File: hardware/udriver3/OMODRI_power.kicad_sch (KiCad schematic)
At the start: 7 parts, among them U7 TMS320F28388D

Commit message: PCB updates. - Replace CAN/RS485 120ohm resistor - Replace resistor on TCAN RXD pin - Update of some references - Add some 3D missing models
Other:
- sheet OMODRI_Alim_12V ports: added none; removed PG_12V0
- sheet OMODRI_Alim_5V ports: added none; removed PG_12V0
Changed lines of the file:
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@@
-    (stroke (width 0) (type default) (color 0 0 0 0))
-  )
-  (wire (pts (xy 49.53 81.28) (xy 58.42 81.28))
     (stroke (width 0) (type default) (color 0 0 0 0))
   )
@@
     )
     (property "Sheet file" "OMODRI_Alim_5V.kicad_sch" (id 1) (at 58.42 88.2146 0)
-      (effects (font (size 1.27 1.27)) (justify left top))
+      (effects (font (size 1.27 1.27)) (justify left top) hide)
     )
     (pin "PG_5V0" output (at 83.82 81.28 0)
       (effects (font (size 1.27 1.27)) (justify right))
-    )
-    (pin "PG_12V0" input (at 58.42 81.28 180)
-      (effects (font (size 1.27 1.27)) (justify left))
     )
   )
@@
     )
     (property "Sheet file" "OMODRI_Alim_3V3.kicad_sch" (id 1) (at 93.98 77.47 0)
-      (effects (font (size 1.27 1.27)) (justify left top))
+      (effects (font (size 1.27 1.27)) (justify left top) hide)
     )
     (pin "PG_5V0" input (at 93.98 76.2 180)
@@
     )
     (property "Sheet file" "OMODRI_Alim_1V2.kicad_sch" (id 1) (at 93.98 87.5796 0)
-      (effects (font (size 1.27 1.27)) (justify left top))
+      (effects (font (size 1.27 1.27)) (justify left top) hide)
     )
     (pin "PG_5V0" input (at 93.98 85.09 180)
@@
     )
     (property "Sheet file" "OMODRI_Alim_REF.kicad_sch" (id 1) (at 93.98 96.52 0)
-      (effects (font (size 1.27 1.27)) (justify left top))
+      (effects (font (size 1.27 1.27)) (justify left top) hide)
     )
   )
@@
     )
     (property "Sheet file" "TMS320_Bypass_Cap.kicad_sch" (id 1) (at 93.98 107.95 0)
-      (effects (font (size 1.27 1.27)) (justify left top))
+      (effects (font (size 1.27 1.27)) (justify left top) hide)
     )
   )
@@
     )
     (property "Sheet file" "OMODRI_Alim_12V.kicad_sch" (id 1) (at 24.13 88.2146 0)
-      (effects (font (size 1.27 1.27)) (justify left top))
-    )
-    (pin "PG_12V0" output (at 49.53 81.28 0)
-      (effects (font (size 1.27 1.27)) (justify right))
-    )
-  )
+      (effects (font (size 1.27 1.27)) (justify left top) hide)
+    )
+  )

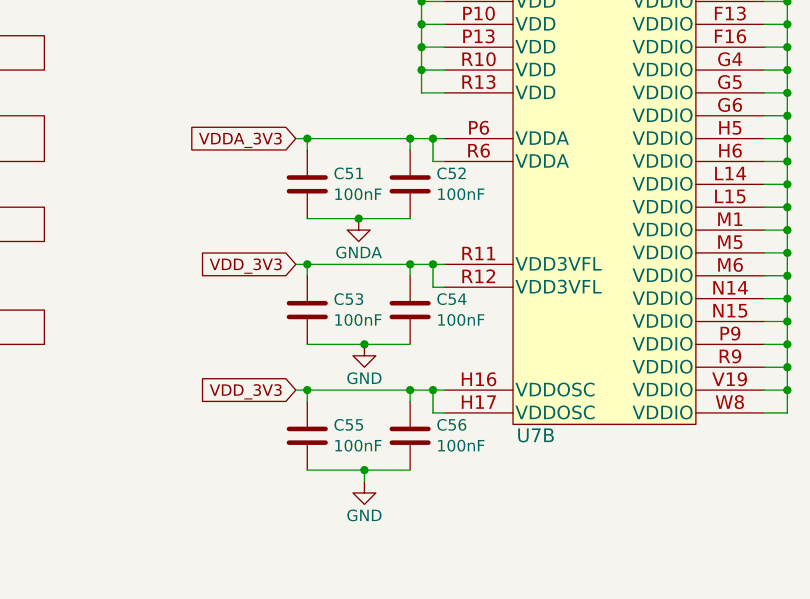
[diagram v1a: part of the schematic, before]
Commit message: PCB updates - FSI protection added against FPC cable reverse connection - BOSCH BMI088 IMU added.
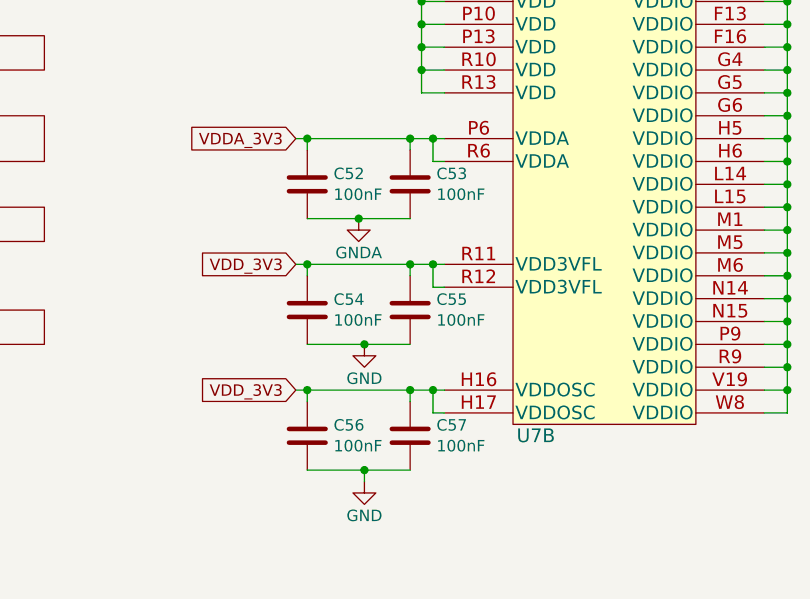
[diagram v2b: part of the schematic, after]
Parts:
- renumbered C51 to C52, C52 to C53, C53 to C54, C54 to C55, C55 to C56, C56 to C57
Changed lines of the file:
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@@
   (title_block
     (title "Open MOtor DRiver Initiative (OMODRI)")
-    (date "2022-10-05")
+    (date "2022-11-24")
     (rev "2.0")
     (company "LAAS/CNRS")
@@
   (symbol (lib_id "power:GND") (at 214.63 143.51 0) (unit 1)
     (in_bom yes) (on_board yes)
-    (property "Reference" "#PWR0122" (id 0) (at 214.63 149.86 0)
+    (property "Reference" "#PWR0123" (id 0) (at 214.63 149.86 0)
       (effects (font (size 1.27 1.27)) hide)
     )
@@
   (symbol (lib_id "power:GND") (at 252.73 143.51 0) (unit 1)
     (in_bom yes) (on_board yes)
-    (property "Reference" "#PWR0123" (id 0) (at 252.73 149.86 0)
+    (property "Reference" "#PWR0124" (id 0) (at 252.73 149.86 0)
       (effects (font (size 1.27 1.27)) hide)
     )
@@
   (symbol (lib_id "power:GND") (at 153.67 107.95 0) (unit 1)
     (in_bom yes) (on_board yes)
-    (property "Reference" "#PWR0120" (id 0) (at 153.67 114.3 0)
+    (property "Reference" "#PWR0121" (id 0) (at 153.67 114.3 0)
       (effects (font (size 1.27 1.27)) hide)
     )
@@
   (symbol (lib_id "power:GND") (at 153.67 123.19 0) (unit 1)
     (in_bom yes) (on_board yes)
-    (property "Reference" "#PWR0121" (id 0) (at 153.67 129.54 0)
+    (property "Reference" "#PWR0122" (id 0) (at 153.67 129.54 0)
       (effects (font (size 1.27 1.27)) hide)
     )
@@
   (symbol (lib_id "power:GNDA") (at 153.035 93.98 0) (unit 1)
     (in_bom yes) (on_board yes)
-    (property "Reference" "#PWR0119" (id 0) (at 153.035 100.33 0)
+    (property "Reference" "#PWR0120" (id 0) (at 153.035 100.33 0)
       (effects (font (size 1.27 1.27)) hide)
     )
@@
   (symbol (lib_id "Device:C") (at 147.32 118.11 0) (unit 1)
     (in_bom yes) (on_board yes)
-    (property "Reference" "C55" (id 0) (at 150.241 116.9416 0)
+    (property "Reference" "C56" (id 0) (at 150.241 116.9416 0)
       (effects (font (size 1.27 1.27)) (justify left))
     )
@@
   (symbol (lib_id "Device:C") (at 147.32 104.14 0) (unit 1)
     (in_bom yes) (on_board yes)
-    (property "Reference" "C53" (id 0) (at 150.241 102.9716 0)
+    (property "Reference" "C54" (id 0) (at 150.241 102.9716 0)
       (effects (font (size 1.27 1.27)) (justify left))
     )
@@
   (symbol (lib_id "Device:C") (at 147.32 90.17 0) (unit 1)
     (in_bom yes) (on_board yes)
-    (property "Reference" "C51" (id 0) (at 150.241 89.0016 0)
+    (property "Reference" "C52" (id 0) (at 150.241 89.0016 0)
       (effects (font (size 1.27 1.27)) (justify left))
     )
@@
   (symbol (lib_id "Device:C") (at 158.75 104.14 0) (unit 1)
     (in_bom yes) (on_board yes)
-    (property "Reference" "C54" (id 0) (at 161.671 102.9716 0)
+    (property "Reference" "C55" (id 0) (at 161.671 102.9716 0)
       (effects (font (size 1.27 1.27)) (justify left))
     )
@@
   (symbol (lib_id "Device:C") (at 158.75 118.11 0) (unit 1)
     (in_bom yes) (on_board yes)
-    (property "Reference" "C56" (id 0) (at 161.671 116.9416 0)
+    (property "Reference" "C57" (id 0) (at 161.671 116.9416 0)
       (effects (font (size 1.27 1.27)) (justify left))
     )
@@
   (symbol (lib_id "Device:C") (at 158.75 90.17 0) (unit 1)
     (in_bom yes) (on_board yes)
-    (property "Reference" "C52" (id 0) (at 161.671 89.0016 0)
+    (property "Reference" "C53" (id 0) (at 161.671 89.0016 0)
       (effects (font (size 1.27 1.27)) (justify left))
     )

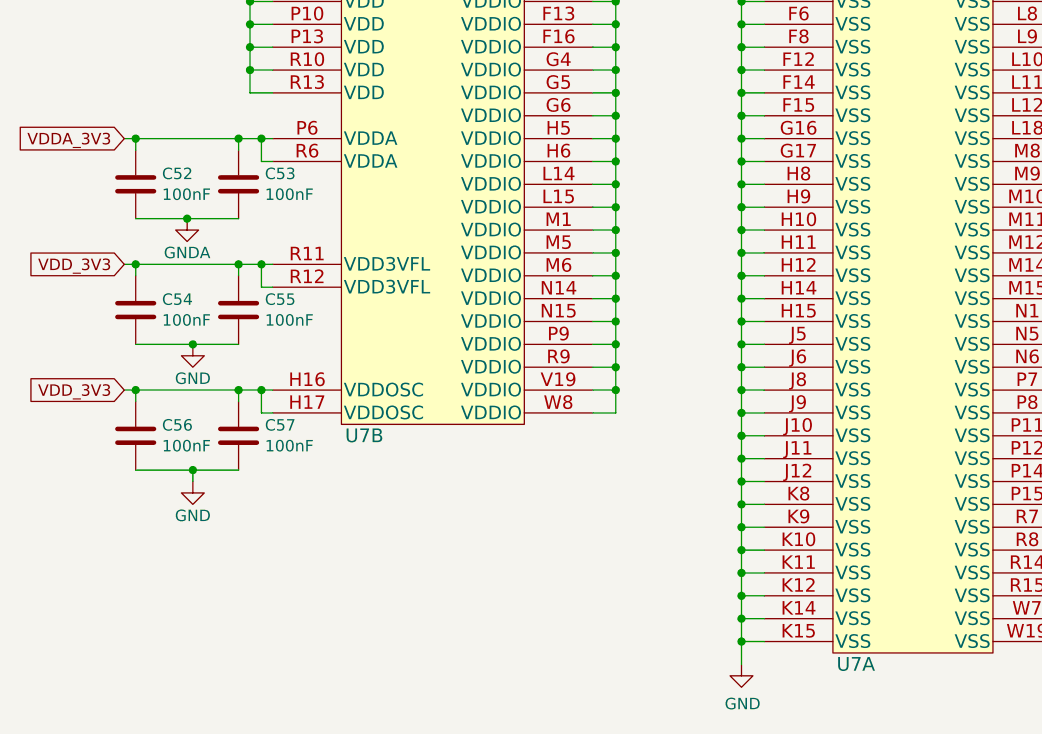
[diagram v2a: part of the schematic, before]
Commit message: PCB udpates. - add serial resistors on boot jumpers - modify config jumpers to be opened by default
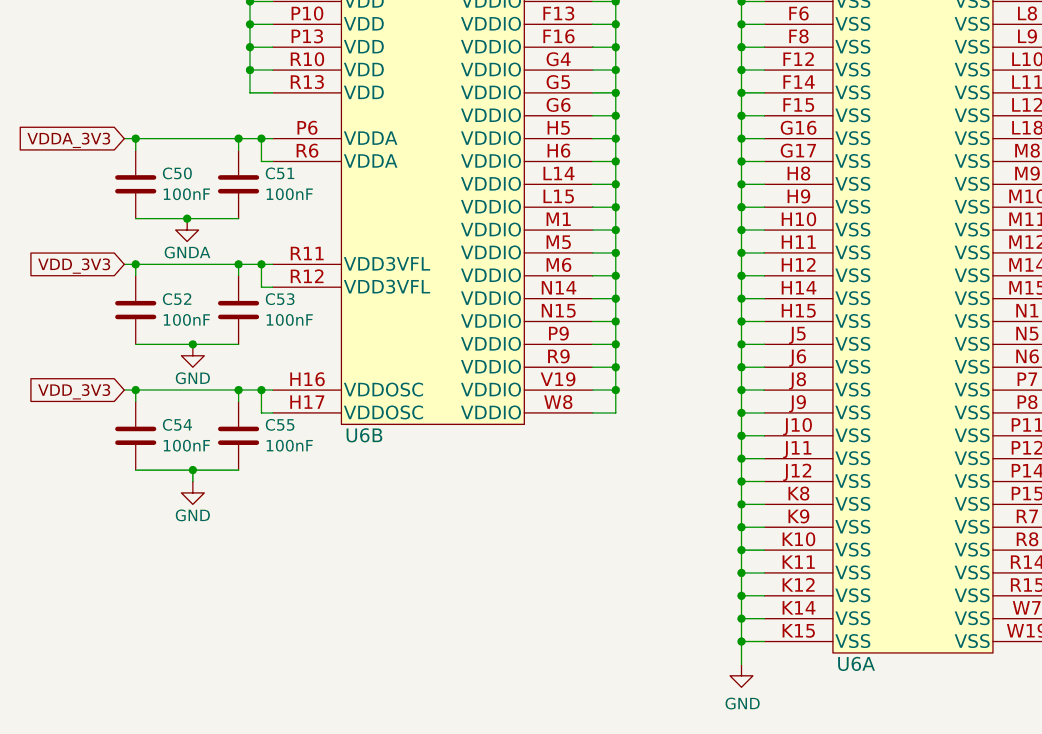
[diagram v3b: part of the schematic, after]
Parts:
- renumbered C52 to C50, C53 to C51, C54 to C52, C55 to C53, C56 to C54, C57 to C55, U7 to U6
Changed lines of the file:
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@@
   (symbol (lib_id "power:GND") (at 214.63 143.51 0) (unit 1)
     (in_bom yes) (on_board yes)
-    (property "Reference" "#PWR0123" (id 0) (at 214.63 149.86 0)
+    (property "Reference" "#PWR0109" (id 0) (at 214.63 149.86 0)
       (effects (font (size 1.27 1.27)) hide)
     )
@@
   (symbol (lib_id "power:GND") (at 252.73 143.51 0) (unit 1)
     (in_bom yes) (on_board yes)
-    (property "Reference" "#PWR0124" (id 0) (at 252.73 149.86 0)
+    (property "Reference" "#PWR0110" (id 0) (at 252.73 149.86 0)
       (effects (font (size 1.27 1.27)) hide)
     )
@@
     (pin "1")
   )
-  (symbol (lib_id "omodri_lib:TMS320F28388D") (at 180.34 95.25 0) (unit 2)
-    (in_bom yes) (on_board yes)
-    (property "Reference" "U7" (id 0) (at 172.72 118.11 0)
+  (symbol (lib_name "TMS320F28388D_1") (lib_id "omodri_lib:TMS320F28388D") (at 180.34 95.25 0) (unit 2)
+    (in_bom yes) (on_board yes)
+    (property "Reference" "U6" (id 0) (at 172.72 118.11 0)
       (effects (font (size 1.524 1.524)))
     )
@@
   (symbol (lib_id "omodri_lib:TMS320F28388D") (at 233.68 95.25 0) (unit 1)
     (in_bom yes) (on_board yes)
-    (property "Reference" "U7" (id 0) (at 227.33 143.51 0)
+    (property "Reference" "U6" (id 0) (at 227.33 143.51 0)
       (effects (font (size 1.524 1.524)))
     )
@@
   (symbol (lib_id "power:GND") (at 153.67 107.95 0) (unit 1)
     (in_bom yes) (on_board yes)
-    (property "Reference" "#PWR0121" (id 0) (at 153.67 114.3 0)
+    (property "Reference" "#PWR0107" (id 0) (at 153.67 114.3 0)
       (effects (font (size 1.27 1.27)) hide)
     )
@@
   (symbol (lib_id "power:GND") (at 153.67 123.19 0) (unit 1)
     (in_bom yes) (on_board yes)
-    (property "Reference" "#PWR0122" (id 0) (at 153.67 129.54 0)
+    (property "Reference" "#PWR0108" (id 0) (at 153.67 129.54 0)
       (effects (font (size 1.27 1.27)) hide)
     )
@@
   (symbol (lib_id "power:GNDA") (at 153.035 93.98 0) (unit 1)
     (in_bom yes) (on_board yes)
-    (property "Reference" "#PWR0120" (id 0) (at 153.035 100.33 0)
+    (property "Reference" "#PWR0106" (id 0) (at 153.035 100.33 0)
       (effects (font (size 1.27 1.27)) hide)
     )
@@
   (symbol (lib_id "Device:C") (at 147.32 118.11 0) (unit 1)
     (in_bom yes) (on_board yes)
-    (property "Reference" "C56" (id 0) (at 150.241 116.9416 0)
+    (property "Reference" "C54" (id 0) (at 150.241 116.9416 0)
       (effects (font (size 1.27 1.27)) (justify left))
     )
@@
   (symbol (lib_id "Device:C") (at 147.32 104.14 0) (unit 1)
     (in_bom yes) (on_board yes)
-    (property "Reference" "C54" (id 0) (at 150.241 102.9716 0)
+    (property "Reference" "C52" (id 0) (at 150.241 102.9716 0)
       (effects (font (size 1.27 1.27)) (justify left))
     )
@@
   (symbol (lib_id "Device:C") (at 147.32 90.17 0) (unit 1)
     (in_bom yes) (on_board yes)
-    (property "Reference" "C52" (id 0) (at 150.241 89.0016 0)
+    (property "Reference" "C50" (id 0) (at 150.241 89.0016 0)
       (effects (font (size 1.27 1.27)) (justify left))
     )
@@
   (symbol (lib_id "Device:C") (at 158.75 104.14 0) (unit 1)
     (in_bom yes) (on_board yes)
-    (property "Reference" "C55" (id 0) (at 161.671 102.9716 0)
+    (property "Reference" "C53" (id 0) (at 161.671 102.9716 0)
       (effects (font (size 1.27 1.27)) (justify left))
     )
@@
   (symbol (lib_id "Device:C") (at 158.75 118.11 0) (unit 1)
     (in_bom yes) (on_board yes)
-    (property "Reference" "C57" (id 0) (at 161.671 116.9416 0)
+    (property "Reference" "C55" (id 0) (at 161.671 116.9416 0)
       (effects (font (size 1.27 1.27)) (justify left))
     )
@@
   (symbol (lib_id "Device:C") (at 158.75 90.17 0) (unit 1)
     (in_bom yes) (on_board yes)
-    (property "Reference" "C53" (id 0) (at 161.671 89.0016 0)
-      (effects (font (size 1.27 1.27)) (justify left))
-    )
+    (property "Reference" "C51" (id 0) (at 161.671 89.0016 0)
+      (effects (font (size 1.27 1.27)) (justify left))
+    )

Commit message: Gerber updates.
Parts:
- U6: DigiKey 296-F28388DZWTS-ND -> 296-F28388DZWTS-ND
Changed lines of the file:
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@@
       (effects (font (size 1.524 1.524)) hide)
     )
-    (property "DigiKey" " 	296-F28388DZWTS-ND" (id 4) (at 180.34 95.25 0)
+    (property "DigiKey" "296-F28388DZWTS-ND" (id 4) (at 180.34 95.25 0)
       (effects (font (size 1.27 1.27)) hide)
     )
@@
       (effects (font (size 1.524 1.524)) hide)
     )
-    (property "DigiKey" " 	296-F28388DZWTS-ND" (id 4) (at 233.68 95.25 0)
+    (property "DigiKey" "296-F28388DZWTS-ND" (id 4) (at 233.68 95.25 0)
       (effects (font (size 1.27 1.27)) hide)
     )

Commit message: Add JLCPCB components ref where it was matching.
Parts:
- C50, C51, C52, C53, C54, C55: LCSC (none) -> C2649540
- U6: LCSC (none) -> C2879671
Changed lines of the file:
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@@
+      (effects (font (size 1.27 1.27)) hide)
+    )
+    (property "LCSC" "C2879671" (at 180.34 95.25 0)
       (effects (font (size 1.27 1.27)) hide)
     )
@@
       (effects (font (size 1.27 1.27)) hide)
     )
+    (property "LCSC" "C2879671" (at 233.68 95.25 0)
+      (effects (font (size 1.27 1.27)) hide)
+    )
     (pin "A1")
     (pin "A10")
@@
       (effects (font (size 1.27 1.27)) hide)
     )
+    (property "LCSC" "C2649540" (at 147.32 118.11 0)
+      (effects (font (size 1.27 1.27)) hide)
+    )
     (pin "1")
     (pin "2")
@@
       (effects (font (size 1.27 1.27)) hide)
     )
+    (property "LCSC" "C2649540" (at 147.32 104.14 0)
+      (effects (font (size 1.27 1.27)) hide)
+    )
     (pin "1")
     (pin "2")
@@
       (effects (font (size 1.27 1.27)) hide)
     )
+    (property "LCSC" "C2649540" (at 147.32 90.17 0)
+      (effects (font (size 1.27 1.27)) hide)
+    )
     (pin "1")
     (pin "2")
@@
       (effects (font (size 1.27 1.27)) hide)
     )
+    (property "LCSC" "C2649540" (at 158.75 104.14 0)
+      (effects (font (size 1.27 1.27)) hide)
+    )
     (pin "1")
     (pin "2")
@@
       (effects (font (size 1.27 1.27)) hide)
     )
+    (property "LCSC" "C2649540" (at 158.75 118.11 0)
+      (effects (font (size 1.27 1.27)) hide)
+    )
     (pin "1")
     (pin "2")
@@
       (effects (font (size 1.27 1.27)) hide)
     )
+    (property "LCSC" "C2649540" (at 158.75 90.17 0)
+      (effects (font (size 1.27 1.27)) hide)
+    )

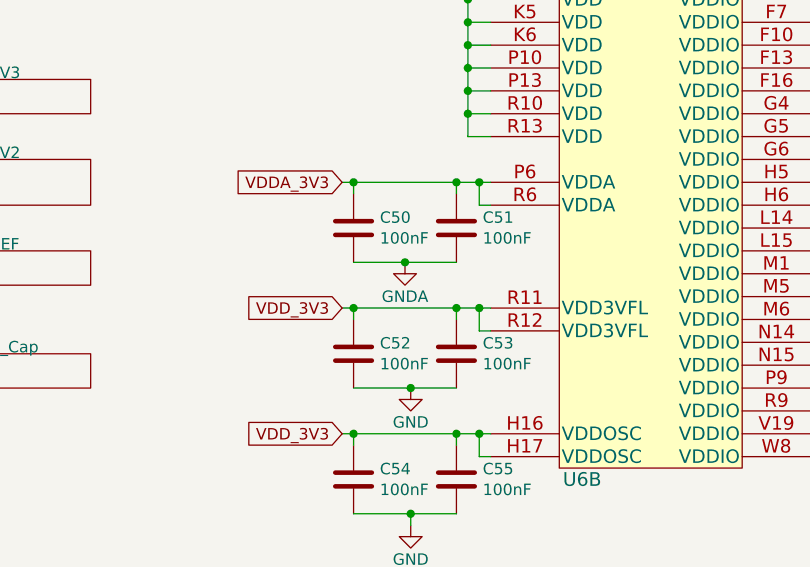
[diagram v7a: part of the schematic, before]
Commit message: Update PCB layout to match JLCPCB requirements (via diameter). Set Netclass constraints defined in uOmodri_v2.
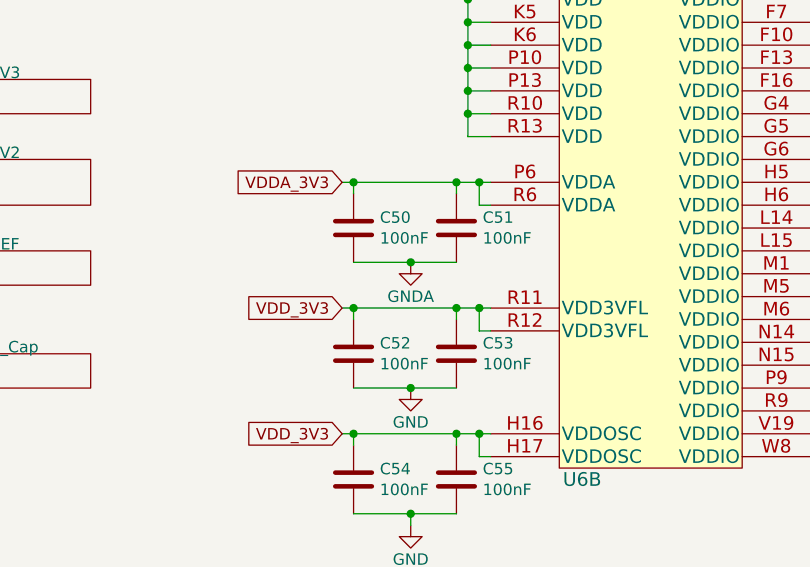
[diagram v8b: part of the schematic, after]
